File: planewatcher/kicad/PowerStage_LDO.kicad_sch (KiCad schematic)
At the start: 11 parts, among them U6 LT3045IMSE-1#PBF

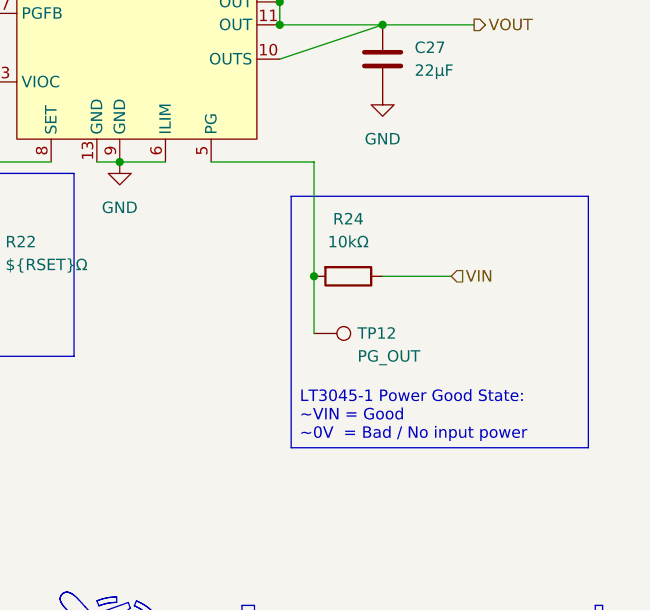
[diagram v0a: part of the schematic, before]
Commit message: Add LDO PG pin to FPGA for monitoring in SW. Add Blinkenlights.
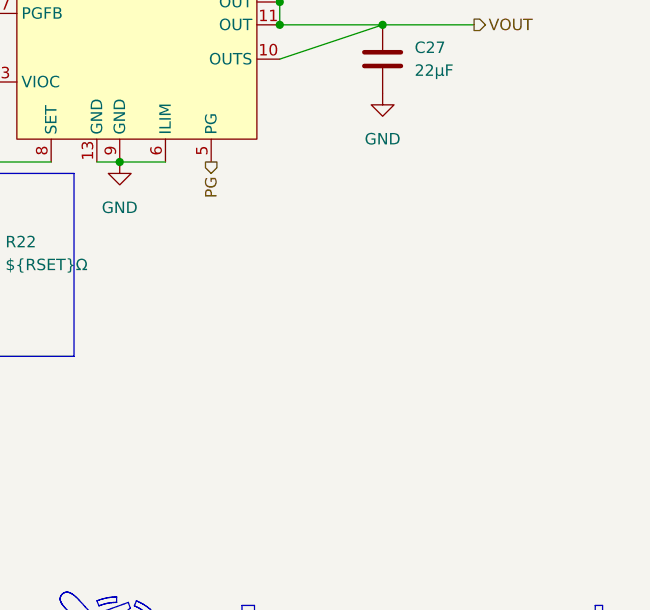
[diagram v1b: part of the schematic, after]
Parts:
- removed R24: 10kΩ, Resistor_SMD:R_0402_1005Metric, symbol Device:R
- removed TP12: PG_OUT, TestPoint:TestPoint_Pad_D1.0mm, symbol Connector:TestPoint
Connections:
- net PG: now reaches U6.5 (PG)

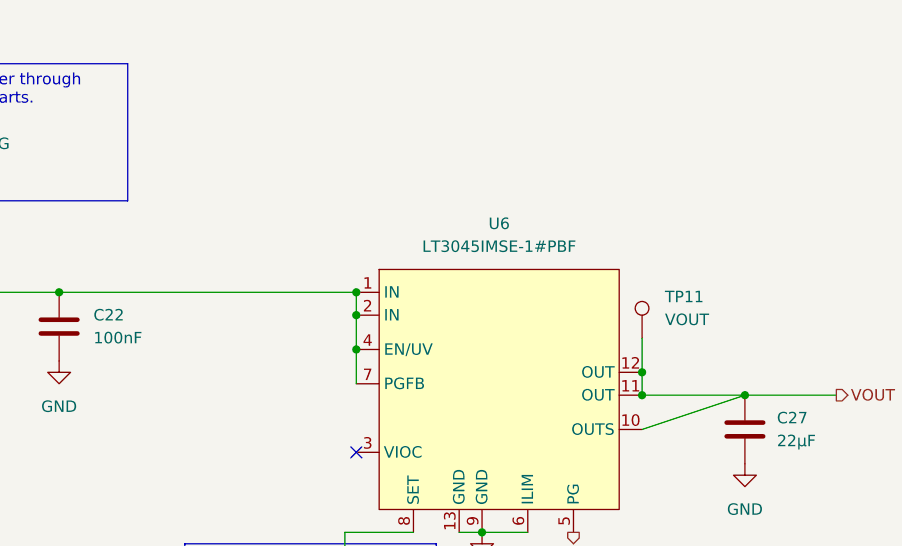
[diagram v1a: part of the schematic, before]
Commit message: Add voltage divider to PGFB to assert PG if 3V3 > ~3.1V. Fix length of AINN net.
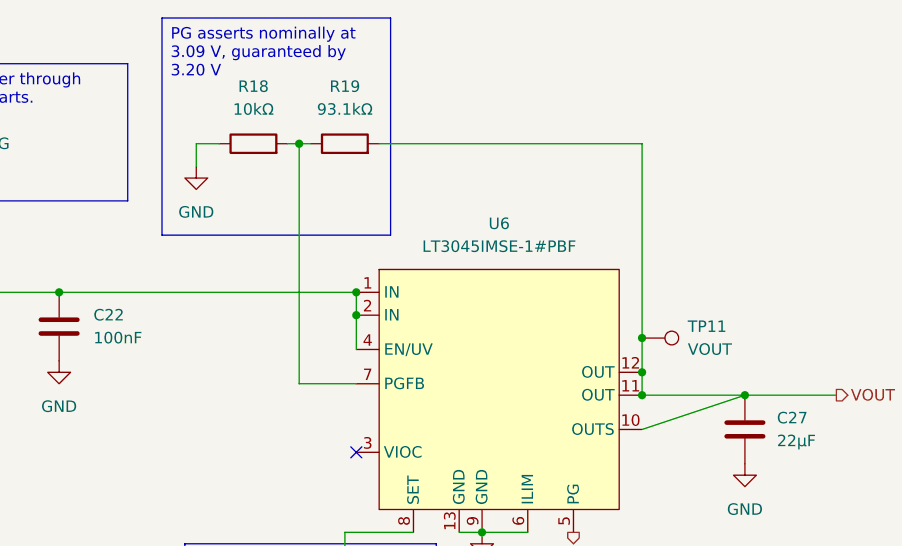
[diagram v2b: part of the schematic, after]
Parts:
- added R18: 10kΩ, Resistor_SMD:R_0402_1005Metric, symbol Device:R
- added R19: 93.1kΩ, Resistor_SMD:R_0402_1005Metric, symbol Device:R
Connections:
- net GND: now also R18.1
- net VOUT: now also R19.2
- net at C21.1, C22.1, L5.2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: no longer U6.7 (PGFB)
- new net: R18.2, R19.1, U6.7 (PGFB)
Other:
- moved on the sheet: TP11

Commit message: Add persistent PCBWay BOM fields to KiCad schematic
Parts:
- C19: MPN (none) -> GRM31CR71E475KA88L; Manufacturer (none) -> Murata; Package (none) -> 1206
- C21: MPN (none) -> GRM31CR71E475KA88L; Manufacturer (none) -> Murata; Package (none) -> 0402
- C22: MPN (none) -> GRM155R71H104KE14D; Manufacturer (none) -> Murata; Package (none) -> 0402
- C26: MPN (none) -> C1608X5R1C475K080AC; Manufacturer (none) -> TDK; Package (none) -> 0402
- C27: MPN (none) -> CL31A226KOHNNNE; Manufacturer (none) -> Samsung; Package (none) -> 0603
- L5: MPN (none) -> BLM21PG601SN1D; Manufacturer (none) -> Murata; Package (none) -> 0805
- R18: MPN (none) -> AT0402BRD0710KL; Manufacturer (none) -> Yageo; Package (none) -> 0402
- R19: MPN (none) -> AT0402BRD0793K1L; Manufacturer (none) -> Yageo; Package (none) -> 0402
- R22: MPN (none) -> RC0402FR-07249RL; Manufacturer (none) -> Yageo; Package (none) -> 0402
- U6: MPN (none) -> LT3045IMSE-1#PBF; Manufacturer (none) -> Analog Devices; Package (none) -> MSOP-12E

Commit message: move power supply and add GPS module
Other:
- title: (none) -> Plane Watcher
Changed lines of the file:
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@@
 	(paper "A4")
 	(title_block
-		(date "2026-05-16")
-		(rev "prototype 1.1")
+		(title "Plane Watcher")
+		(date "2026-05-18")
+		(rev "prototype 1.2")
 		(company "plane.watch")
 	)
@@
 			)
 		)
-			(property "Datasheet" ""
+		(property "Datasheet" ""
 			(at 234.95 85.09 0)
 			(hide yes)

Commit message: review & consolidate all capacitors
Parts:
- C19: MPN GRM31CR71E475KA88L -> GCJ31CR71C475KA01L; Manufacturer Murata -> Murata Electronics; Package 1206 -> 1206 (3216 Metric); Purpose Input/pre-regulator ceramic capacitor for the LT8608 buck s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 -> Bulk Input capacitor for the LT3045-1.; Suggested Part Murata GRM31CR71E475KA88L -> (none)
- C21: MPN GRM31CR71E475KA88L -> GCJ31CR71C475KA01L; Manufacturer Murata -> Murata Electronics; Package 0402 -> 1206 (3216 Metric); Purpose Input/pre-regulator ceramic capacitor for the LT8608 buck s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 -> Low freq bypass capacitor for the LT3045-1.; Suggested Part Murata GRM31CR71E475KA88L -> (none)
- C22: MPN GRM155R71H104KE14D -> GCM155R71A104KA55D; Manufacturer Murata -> Murata Electronics; Package 0402 -> 0402 (1005 Metric); Purpose High-frequency bypass capacitor for the LT8608/LT3045 suppl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 -> High freq bypass capacitor for the LT3045-1.; Suggested Part Murata GRM155R71H104KE14D -> (none)
- C26: MPN C1608X5R1C475K080AC -> GRM188Z71A475KE15D; Manufacturer TDK -> Murata Electronics; Package 0402 -> 0603 (1608 Metric); Suggested Part TDK C1608X5R1C475K080AC -> (none)
- C27: Design Notes (none) -> ~18µF after DC bias de-rating; MPN CL31A226KOHNNNE -> GCJ31CR71A226KE01K; Manufacturer Samsung -> Murata Electronics; Package 0603 -> 1206 (3216 Metric); Suggested Part Samsung CL31A226KOHNNNE -> (none)
- L5: Suggested Part Murata BLM21PG601SN1D -> (none)
- R18: Suggested Part Yageo AT0402BRD0710KL -> (none)
- R19: Suggested Part Yageo AT0402BRD0793K1L -> (none)
- R22: Suggested Part ${RSET_Suggested_Part} -> (none)
- TP11: Suggested Part No fitted part (PCB pad only) -> (none)
- U6: Suggested Part Analog Devices LT3045IMSE-1#PBF -> (none)
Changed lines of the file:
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@@
-			)
-		)
-		(property "Suggested Part" "Murata BLM21PG601SN1D"
-			(at 128.27 66.04 0)
-			(hide yes)
-			(show_name no)
-			(do_not_autoplace no)
-			(effects
-				(font
-					(size 1.27 1.27)
-				)
 			)
 		)
 		(property "Purpose" "Filters high-frequency switching noise on the low-noise regulator rail."
 			(at 128.27 66.04 0)
+			(hide yes)
+			(show_name no)
+			(do_not_autoplace no)
+			(effects
+				(font
+					(size 1.27 1.27)
+				)
+			)
+		)
+		(property "Mount_Type" ""
+			(at 128.27 66.04 90)
 			(hide yes)
 			(show_name no)
@@
 			)
 		)
-		(property "Datasheet" ""
+		(property "Datasheet" "https://www.murata.com/en-sg/api/pdfdownloadapi?cate=luCeramicCapacitorsSMD&partno=GCJ31CR71C475KA01%23"
 			(at 138.43 69.85 0)
 			(hide yes)
@@
 			)
 		)
-		(property "Description" "4.7µF, X7R, ±10%, 25V, 1206 MLCC"
+		(property "Description" "4.7 µF ±10% 16V Ceramic Capacitor X7R 1206 (3216 Metric)"
 			(at 138.43 69.85 0)
 			(hide yes)
@@
 			)
 		)
-		(property "Package" "0402"
+		(property "Package" "1206 (3216 Metric)"
 			(at 138.43 69.85 0)
 			(hide yes)
@@
 			)
 		)
-		(property "MPN" "GRM31CR71E475KA88L"
+		(property "MPN" "GCJ31CR71C475KA01L"
 			(at 138.43 69.85 0)
 			(hide yes)
@@
 			)
 		)
-		(property "Manufacturer" "Murata"
+		(property "Manufacturer" "Murata Electronics"
 			(at 138.43 69.85 0)
 			(hide yes)
@@
 			)
 		)
-		(property "Suggested Part" "Murata GRM31CR71E475KA88L"
+		(property "Purpose" "Low freq bypass capacitor for the LT3045-1."
 			(at 138.43 69.85 0)
 			(hide yes)
@@
 			)
 		)
-		(property "Purpose" "Input/pre-regulator ceramic capacitor for the LT8608 buck stage."
+		(property "Mount_Type" ""
 			(at 138.43 69.85 0)
 			(hide yes)
@@
 			)
 		)
-		(property "Suggested Part" "No fitted part (PCB pad only)"
-			(at 223.52 71.12 0)
-			(hide yes)
-			(show_name no)
-			(do_not_autoplace no)
-			(effects
-				(font
-					(size 1.27 1.27)
-				)
-			)
-		)
 		(property "Purpose" "Provides oscilloscope/DMM probe access to VOUT."
 			(at 223.52 71.12 0)
@@
 		(property "Notes" "Expected voltage: VOUT."
 			(at 223.52 71.12 0)
+			(hide yes)
+			(show_name no)
+			(do_not_autoplace no)
+			(effects
+				(font
+					(size 1.27 1.27)
+				)
+			)
+		)
+		(property "Mount_Type" ""
+			(at 223.52 71.12 90)
 			(hide yes)
 			(show_name no)
@@
 			)
 		)
-		(property "Datasheet" ""
+		(property "Datasheet" "https://pim.murata.com/en-sg/pim/details/?partNum=GCJ31CR71A226KE01%23&displayChangeClass=productDetailPrint"
 			(at 234.95 81.28 0)
 			(hide yes)
@@
 			)
 		)
-		(property "Description" "22µF, X5R, ±10%, 16V, 1206 MLCC"
+		(property "Description" "22 µF ±10% 10V Ceramic Capacitor X7R 1206 (3216 Metric)"
 			(at 234.95 81.28 0)
 			(hide yes)
@@
 			)
 		)
-		(property "Package" "0603"
+		(property "Package" "1206 (3216 Metric)"
 			(at 234.95 81.28 0)
 			(hide yes)
@@
 			)
 		)
-		(property "MPN" "CL31A226KOHNNNE"
+		(property "MPN" "GCJ31CR71A226KE01K"
 			(at 234.95 81.28 0)
 			(hide yes)
@@
 			)
 		)
-		(property "Manufacturer" "Samsung"
-			(at 234.95 81.28 0)
-			(hide yes)
-			(show_name no)
-			(do_not_autoplace no)
-			(effects
-				(font
-					(size 1.27 1.27)
-				)
-			)
-		)
-		(property "Suggested Part" "Samsung CL31A226KOHNNNE"
+		(property "Manufacturer" "Murata Electronics"
 			(at 234.95 81.28 0)
 			(hide yes)
@@
 		)
 		(property "Notes" ""
+			(at 234.95 81.28 0)
+			(hide yes)
+			(show_name no)
+			(do_not_autoplace no)
+			(effects
+				(font
+					(size 1.27 1.27)
+				)
+			)
+		)
+		(property "Mount_Type" ""
+			(at 234.95 81.28 0)
+			(hide yes)
+			(show_name no)
+			(do_not_autoplace no)
+			(effects
+				(font
+					(size 1.27 1.27)
+				)
+			)
+		)
+		(property "Design Notes" "~18µF after DC bias de-rating"
 			(at 234.95 81.28 0)
 			(hide yes)
@@
 			)
 		)
-		(property "Suggested Part" "${RSET_Suggested_Part}"
-			(at 190.5 102.87 0)
-			(hide yes)
-			(show_name no)
-			(do_not_autoplace no)
-			(effects
-				(font
-					(size 1.27 1.27)
-				)
-			)
-		)
 		(property "Purpose" "Sets the LT3045 output voltage through the 100µA SET pin reference."
 			(at 190.5 102.87 0)
@@
 		)
 		(property "Notes" "LT3045 SET resistor, 0.1% thin film, ≤25ppm/°C, 0603, sets VOUT via 100µA reference"
+			(at 190.5 102.87 0)
+			(hide yes)
+			(show_name no)
+			(do_not_autoplace no)
+			(effects
+				(font
+					(size 1.27 1.27)
+				)
+			)
+		)
+		(property "Mount_Type" ""
 			(at 190.5 102.87 0)
 			(hide yes)
@@
 			)
 		)
-		(property "Suggested Part" "Yageo AT0402BRD0710KL"
+		(property "Purpose" "Lower resistor in the LT3045 PGFB divider; sets the power-good assertion threshold."
 			(at 180.34 49.53 90)
 			(hide yes)
@@
 			)
 		)
-		(property "Purpose" "Lower resistor in the LT3045 PGFB divider; sets the power-good assertion threshold."
+		(property "Mount_Type" ""
 			(at 180.34 49.53 90)
 			(hide yes)
@@
 			)
 		)
-		(property "Suggested Part" "Analog Devices LT3045IMSE-1#PBF"
-			(at 207.01 58.42 0)
-			(hide yes)
-			(show_name no)
-			(do_not_autoplace no)
-			(effects
-				(font
-					(size 1.27 1.27)
-				)
-			)
-		)
 		(property "Purpose" "Post-regulates the buck output to the low-noise analog/RF/digital rail."
 			(at 207.01 58.42 0)
@@
 		)
 		(property "Notes" "From datasheet: \"For optimal transient performance and load regulation, Kelvin connect OUTS directly to the output capacitor and the load. Also, tie the GND connections of the output capacitor and the SET pin capacitor directly together .\""
+			(at 207.01 58.42 0)
+			(hide yes)
+			(show_name no)
+			(do_not_autoplace no)
+			(effects
+				(font
+					(size 1.27 1.27)
+				)
+			)
+		)
+		(property "Mount_Type" ""
 			(at 207.01 58.42 0)
 			(hide yes)
@@
 			)
 		)
-		(property "Datasheet" ""
+		(property "Datasheet" "https://www.murata.com/en-sg/api/pdfdownloadapi?cate=luCeramicCapacitorsSMD&partno=GCJ31CR71C475KA01%23"
 			(at 118.11 69.85 0)
 			(hide yes)
@@
 			)
 		)
-		(property "Description" "4.7µF, X7R, ±10%, 25V, 1206 MLCC"
+		(property "Description" "4.7 µF ±10% 16V Ceramic Capacitor X7R 1206 (3216 Metric)"
 			(at 118.11 69.85 0)
 			(hide yes)
@@
 			)
 		)
-		(property "Package" "1206"
+		(property "Package" "1206 (3216 Metric)"
 			(at 118.11 69.85 0)
 			(hide yes)
@@
 			)
 		)
-		(property "MPN" "GRM31CR71E475KA88L"
+		(property "MPN" "GCJ31CR71C475KA01L"
 			(at 118.11 69.85 0)
 			(hide yes)
@@
 			)
 		)
-		(property "Manufacturer" "Murata"
+		(property "Manufacturer" "Murata Electronics"
 			(at 118.11 69.85 0)
 			(hide yes)
@@
 			)
 		)
-		(property "Suggested Part" "Murata GRM31CR71E475KA88L"
+		(property "Purpose" "Bulk Input capacitor for the LT3045-1."
 			(at 118.11 69.85 0)
 			(hide yes)
@@
 			)
 		)
-		(property "Purpose" "Input/pre-regulator ceramic capacitor for the LT8608 buck stage."
+		(property "Mount_Type" ""
 			(at 118.11 69.85 0)
 			(hide yes)
@@
 			)
 		)
-		(property "Datasheet" ""
+		(property "Datasheet" "https://search.murata.co.jp/Ceramy/image/img/A01X/G101/ENG/GRM188Z71A475KE15-01.pdf"
 			(at 177.8 102.87 0)
 			(hide yes)
@@
 			)
 		)
-		(property "Description" "4.7µF, X5R, ±10%, 16V, 0603 MLCC"
+		(property "Description" "4.7 µF ±10% 10V Ceramic Capacitor X7R 0603 (1608 Metric)"
 			(at 177.8 102.87 0)
 			(hide yes)
@@
 			)
 		)
-		(property "Package" "0402"
+		(property "Package" "0603 (1608 Metric)"
 			(at 177.8 102.87 0)
 			(hide yes)
@@
 			)
 		)
-		(property "MPN" "C1608X5R1C475K080AC"
+		(property "MPN" "GRM188Z71A475KE15D"
 			(at 177.8 102.87 0)
 			(hide yes)
@@
 			)
 		)
-		(property "Manufacturer" "TDK"
-			(at 177.8 102.87 0)
-			(hide yes)
-			(show_name no)
-			(do_not_autoplace no)
-			(effects
-				(font
-					(size 1.27 1.27)
-				)
-			)
-		)
-		(property "Suggested Part" "TDK C1608X5R1C475K080AC"
+		(property "Manufacturer" "Murata Electronics"
 			(at 177.8 102.87 0)
 			(hide yes)
@@
 		)
 		(property "Notes" ""
+			(at 177.8 102.87 0)
+			(hide yes)
+			(show_name no)
+			(do_not_autoplace no)
+			(effects
+				(font
+					(size 1.27 1.27)
+				)
+			)
+		)
+		(property "Mount_Type" ""
 			(at 177.8 102.87 0)
 			(hide yes)
@@
 			)
 		)
-		(property "Datasheet" ""
+		(property "Datasheet" "https://search.murata.co.jp/Ceramy/image/img/A01X/G101/ENG/GCM155R71A104KA55-01.pdf"
 			(at 158.75 69.85 0)
 			(hide yes)
@@
 			)
 		)
-		(property "Description" "100nF, X7R, ±10%, 50V, 0402 MLCC"
+		(property "Description" "0.1 µF ±10% 10V Ceramic Capacitor X7R 0402 (1005 Metric)"
 			(at 158.75 69.85 0)
 			(hide yes)
@@
 			)
 		)
-		(property "Package" "0402"
+		(property "Package" "0402 (1005 Metric)"
 			(at 158.75 69.85 0)
 			(hide yes)
@@
 			)
 		)
-		(property "MPN" "GRM155R71H104KE14D"
+		(property "MPN" "GCM155R71A104KA55D"
 			(at 158.75 69.85 0)
 			(hide yes)
@@
 			)
 		)
-		(property "Manufacturer" "Murata"
+		(property "Manufacturer" "Murata Electronics"
 			(at 158.75 69.85 0)
 			(hide yes)
@@
 			)
 		)
-		(property "Suggested Part" "Murata GRM155R71H104KE14D"
+		(property "Purpose" "High freq bypass capacitor for the LT3045-1."
 			(at 158.75 69.85 0)
 			(hide yes)
@@
 			)
 		)
-		(property "Purpose" "High-frequency bypass capacitor for the LT8608/LT3045 supply path."
+		(property "Mount_Type" ""
 			(at 158.75 69.85 0)
 			(hide yes)
@@
 			)
 		)
-		(property "Suggested Part" "Yageo AT0402BRD0793K1L"
-			(at 190.5 49.53 90)
-			(hide yes)
-			(show_name no)
-			(do_not_autoplace no)
-			(effects
-				(font
-					(size 1.27 1.27)
-				)
-			)
-		)
 		(property "Purpose" "Upper resistor in the LT3045 PGFB divider; sets the power-good assertion threshold."
 			(at 190.5 49.53 90)
 			(hide yes)
+			(show_name no)
+			(do_not_autoplace no)
+			(effects
+				(font
+					(size 1.27 1.27)
+				)
+			)
+		)
+		(property "Mount_Type" ""
+			(at 190.5 49.53 90)
+			(hide yes)

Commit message: review & consolidate all resistors
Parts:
- R18: MPN AT0402BRD0710KL -> ERA-2AEB103X; Manufacturer Yageo -> Panasonic Industry; Package 0402 -> 0402 (1005 Metric)
- R19: MPN AT0402BRD0793K1L -> ERA-2AEB9312X; Manufacturer Yageo -> Panasonic Industry; Package 0402 -> 0402 (1005 Metric)
- R22: value ${RSET}Ω -> 33.2kΩ; MPN RC0402FR-07249RL -> ERA-3ARB3322V; Manufacturer Yageo -> Panasonic Industry; Notes LT3045 SET resistor, 0.1% thin film, ≤25ppm/°C, 0603, sets 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 -> (none); Package 0402 -> 0603 (1608 Metric)
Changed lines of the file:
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@@
 			)
 		)
-		(property "Value" "${RSET}Ω"
+		(property "Value" "33.2kΩ"
 			(at 193.04 104.1399 0)
 			(show_name no)
@@
 			)
 		)
-		(property "Datasheet" "https://industrial.panasonic.com/ww/products/pt/high-precision-chip-resistors/models/ERA3AEB3322V"
+		(property "Datasheet" "https://industrial.panasonic.com/cdbs/www-data/pdf/RDM0000/AOA0000C307.pdf"
 			(at 190.5 102.87 0)
 			(hide yes)
@@
 			)
 		)
-		(property "Description" "${RSET}Ω, ±0.1%, thin film, ≤25ppm/°C, 0603 LT3045 SET resistor"
+		(property "Description" "33.2 kOhms ±0.1% 0.1W, 1/10W Chip Resistor 0603 (1608 Metric) Automotive AEC-Q200 Thin Film"
 			(at 190.5 102.87 0)
 			(hide yes)
@@
 			)
 		)
-		(property "Package" "0402"
+		(property "Package" "0603 (1608 Metric)"
 			(at 190.5 102.87 0)
 			(hide yes)
@@
 			)
 		)
-		(property "MPN" "RC0402FR-07249RL"
+		(property "MPN" "ERA-3ARB3322V"
 			(at 190.5 102.87 0)
 			(hide yes)
@@
 			)
 		)
-		(property "Manufacturer" "Yageo"
+		(property "Manufacturer" "Panasonic Industry"
 			(at 190.5 102.87 0)
 			(hide yes)
@@
 		)
 		(property "Purpose" "Sets the LT3045 output voltage through the 100µA SET pin reference."
-			(at 190.5 102.87 0)
-			(hide yes)
-			(show_name no)
-			(do_not_autoplace no)
-			(effects
-				(font
-					(size 1.27 1.27)
-				)
-			)
-		)
-		(property "Notes" "LT3045 SET resistor, 0.1% thin film, ≤25ppm/°C, 0603, sets VOUT via 100µA reference"
-			(at 190.5 102.87 0)
-			(hide yes)
-			(show_name no)
-			(do_not_autoplace no)
-			(effects
-				(font
-					(size 1.27 1.27)
-				)
-			)
-		)
-		(property "Mount_Type" ""
 			(at 190.5 102.87 0)
 			(hide yes)
@@
 			)
 		)
-		(property "Datasheet" "https://www.yageogroup.com/component-documentation/download/specsheet/AT0402BRD0710KL"
+		(property "Datasheet" "https://industrial.panasonic.com/cdbs/www-data/pdf/RDM0000/AOA0000C307.pdf"
 			(at 180.34 49.53 0)
 			(hide yes)
@@
 			)
 		)
-		(property "Description" "10kΩ, ±0.1%, thin film, ±25ppm/°C, 0402 chip resistor"
+		(property "Description" "10 kOhms ±0.1% 0.063W, 1/16W Chip Resistor 0402 (1005 Metric) Automotive AEC-Q200 Thin Film"
 			(at 180.34 49.53 0)
 			(hide yes)
@@
 			)
 		)
-		(property "Package" "0402"
+		(property "Package" "0402 (1005 Metric)"
 			(at 180.34 49.53 0)
 			(hide yes)
@@
 			)
 		)
-		(property "MPN" "AT0402BRD0710KL"
+		(property "MPN" "ERA-2AEB103X"
 			(at 180.34 49.53 0)
 			(hide yes)
@@
 			)
 		)
-		(property "Manufacturer" "Yageo"
+		(property "Manufacturer" "Panasonic Industry"
 			(at 180.34 49.53 0)
 			(hide yes)
@@
 			)
 		)
-		(property "Datasheet" "https://www.yageogroup.com/component-documentation/download/specsheet/AT0402BRD0793K1L"
+		(property "Datasheet" "https://industrial.panasonic.com/cdbs/www-data/pdf/RDM0000/AOA0000C307.pdf"
 			(at 190.5 49.53 0)
 			(hide yes)
@@
 			)
 		)
-		(property "Description" "93.1kΩ, ±0.1%, thin film, ±25ppm/°C, 0402 chip resistor"
+		(property "Description" "93.1 kOhms ±0.1% 0.063W, 1/16W Chip Resistor 0402 (1005 Metric) Automotive AEC-Q200 Thin Film"
 			(at 190.5 49.53 0)
 			(hide yes)
@@
 			)
 		)
-		(property "Package" "0402"
+		(property "Package" "0402 (1005 Metric)"
 			(at 190.5 49.53 0)
 			(hide yes)
@@
 			)
 		)
-		(property "MPN" "AT0402BRD0793K1L"
+		(property "MPN" "ERA-2AEB9312X"
 			(at 190.5 49.53 0)
 			(hide yes)
@@
 			)
 		)
-		(property "Manufacturer" "Yageo"
+		(property "Manufacturer" "Panasonic Industry"
 			(at 190.5 49.53 0)
 			(hide yes)
